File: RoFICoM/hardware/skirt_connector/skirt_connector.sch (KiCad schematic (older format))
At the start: 17 parts, among them J1 Cable, J10 SENSE_1, J11 SENSE_2, J12 48V_B, J13 48V_2, J14 GND_B, J15 GND_2, J16 RX_B, J17 TX_2, J2 48V_A, J3 48V_1, J4 GND_A, J5 GND_1, J6 RX_A, J7 TX_1, J8 SENSE_A, J9 SENSE_B

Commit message: RoFICoM: Add version 0.2 of the skirt PCB
- add VL53L1X distance sensor
- use flat ribbon cable for connection to the control board
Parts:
- added C1: 470n, Capacitor_SMD:C_0402_1005Metric, symbol Device:C
- added C2: 100n, Capacitor_SMD:C_0402_1005Metric, symbol Device:C
- added R1, R2, R3: 10k, Resistor_SMD:R_0402_1005Metric, symbol Device:R
- added U1: VL53L1X, rofi:VL53L1X_handsoldering, symbol rofi:VL53L1X
- J1: footprint rofi:skirt_8_pin -> rofi:flat_cable_9; symbol Connector:Conn_01x08_Male -> Connector:Conn_01x09_Male
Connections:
- net GND: now also J1.1 (Pin_1), C1.2, C2.2, R1.2, R3.2, U1.12 (GND), U1.2 (AVSSVCSEL), U1.3 (GND), U1.4 (GND), U1.6 (GND); no longer J1.6 (Pin_6)
- net RX: now also J1.4 (Pin_4); no longer J1.1 (Pin_1)
- net S_A_PIN: now also J1.5 (Pin_5); no longer J1.2 (Pin_2)
- net S_B_PIN: now also J1.2 (Pin_2); no longer J1.8 (Pin_8)
- net TX: now also J1.3 (Pin_3); no longer J1.4 (Pin_4)
- net 48V renamed +48V
- net +48V: now also J1.9 (Pin_9); no longer J1.5 (Pin_5)
- net S_1_PAD: no longer names the net of J10.1 (Pin_1)
- net S_1_PAD: now also R2.1; no longer J1.3 (Pin_3)
- net S_2_PAD: no longer names the net of J11.1 (Pin_1)
- net S_2_PAD: now also R3.1; no longer J1.7 (Pin_7)
- new net: R1.1, U1.5 (~SHUT)
- new net +3V3: C1.1, C2.1, J1.6 (Pin_6), R2.2, U1.1 (AVDDVCSEL), U1.11 (AVDD)
- new net SCL: J1.7 (Pin_7), U1.10 (SCL)
- new net SDA: J1.8 (Pin_8), U1.9 (SDA)
- no-connect marks 0 -> 1

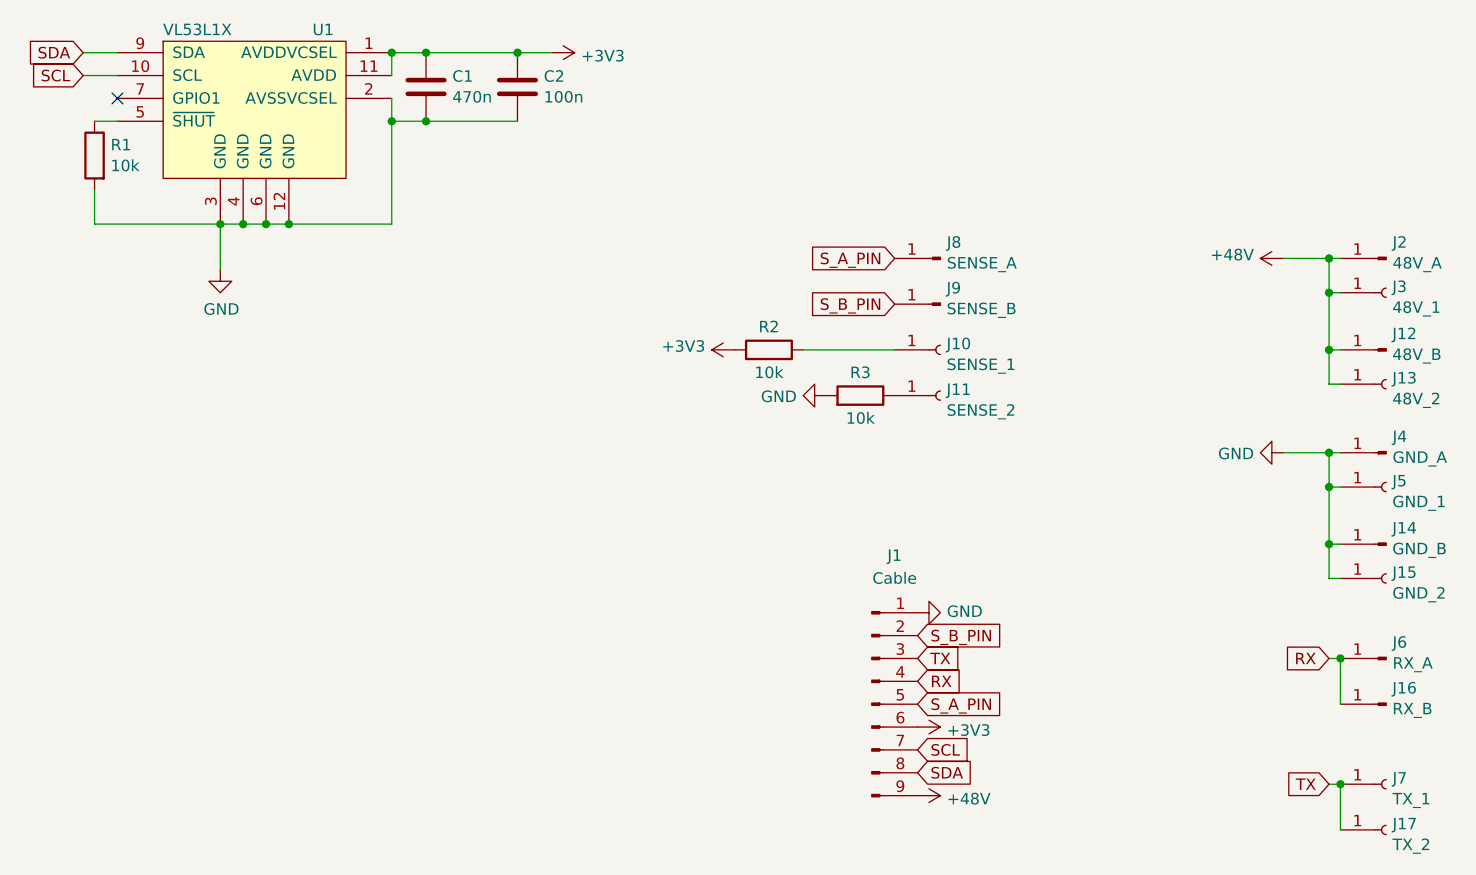
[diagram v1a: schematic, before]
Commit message: RoFICoM: Add missing order codes for the skirt connector
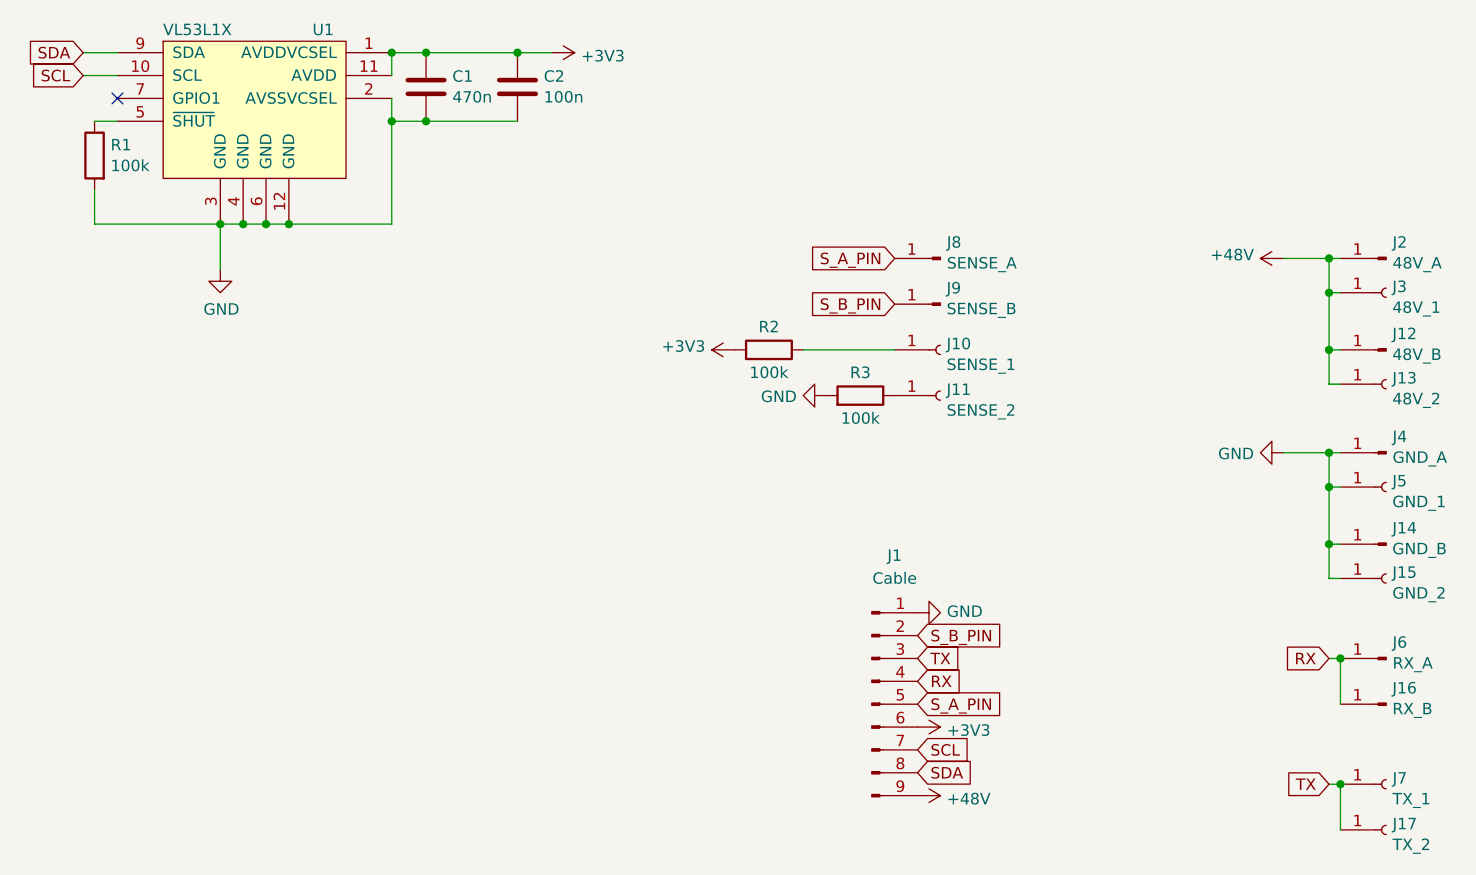
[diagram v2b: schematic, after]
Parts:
- C1: manf# (none) -> CC0402ZRY5V6BB474
- C2: manf# (none) -> CC0402KRX5R6BB104
- R1, R2, R3: value 10k -> 100k; manf# (none) -> RC0402JR-13100KL
- U1: manf# (none) -> VL53L1CXV0FY/1
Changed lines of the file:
@@
 EESchema Schematic File Version 4
 LIBS:skirt_connector-cache
-EELAYER 26 0
+EELAYER 29 0
 EELAYER END
 $Descr A4 11693 8268
@@
 F 2 "rofi:VL53L1X_handsoldering" H 2450 1450 50  0001 C CNN
 F 3 "" H 2450 1450 50  0001 C CNN
+F 4 "VL53L1CXV0FY/1" H 0   0   50  0001 C CNN "manf#"
 	1    2450 1450
 	1    0    0    -1
@@
 P 1750 1750
 F 0 "R1" H 1680 1796 50  0000 R CNN
-F 1 "10k" H 1680 1705 50  0000 R CNN
+F 1 "100k" H 1680 1705 50  0000 R CNN
 F 2 "Resistor_SMD:R_0402_1005Metric" V 1680 1750 50  0001 C CNN
 F 3 "~" H 1750 1750 50  0001 C CNN
+F 4 "RC0402JR-13100KL" H 0   0   50  0001 C CNN "manf#"
 	1    1750 1750
 	-1   0    0    -1
@@
 F 2 "Capacitor_SMD:C_0402_1005Metric" H 3238 1300 50  0001 C CNN
 F 3 "~" H 3200 1450 50  0001 C CNN
+F 4 "CC0402ZRY5V6BB474" H 0   0   50  0001 C CNN "manf#"
 	1    3200 1450
 	1    0    0    -1
@@
 F 2 "Capacitor_SMD:C_0402_1005Metric" H 3638 1300 50  0001 C CNN
 F 3 "~" H 3600 1450 50  0001 C CNN
+F 4 "CC0402KRX5R6BB104" H 0   0   50  0001 C CNN "manf#"
 	1    3600 1450
 	1    0    0    -1
@@
 P 4700 2600
 F 0 "R2" V 4800 2600 50  0000 C CNN
-F 1 "10k" V 4600 2600 50  0000 C CNN
+F 1 "100k" V 4600 2600 50  0000 C CNN
 F 2 "Resistor_SMD:R_0402_1005Metric" V 4630 2600 50  0001 C CNN
 F 3 "~" H 4700 2600 50  0001 C CNN
+F 4 "RC0402JR-13100KL" H 0   0   50  0001 C CNN "manf#"
 	1    4700 2600
 	0    1    -1   0
@@
 P 5100 2800
 F 0 "R3" V 5200 2800 50  0000 C CNN
-F 1 "10k" V 5000 2800 50  0000 C CNN
+F 1 "100k" V 5000 2800 50  0000 C CNN
 F 2 "Resistor_SMD:R_0402_1005Metric" V 5030 2800 50  0001 C CNN
 F 3 "~" H 5100 2800 50  0001 C CNN
+F 4 "RC0402JR-13100KL" H 0   0   50  0001 C CNN "manf#"
 	1    5100 2800
 	0    1    -1   0

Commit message: RoFICoM: Move cable to the bottom side of skirt connector
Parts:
- J1: footprint rofi:flat_cable_9 -> rofi:flat_cable_9_smd
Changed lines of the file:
@@
 F 0 "J1" H 5250 4800 50  0000 C CNN
 F 1 "Cable" H 5250 4700 50  0000 C CNN
-F 2 "rofi:flat_cable_9" H 5150 4150 50  0001 C CNN
+F 2 "rofi:flat_cable_9_smd" H 5150 4150 50  0001 C CNN
 F 3 "~" H 5150 4150 50  0001 C CNN
 	1    5150 4150
